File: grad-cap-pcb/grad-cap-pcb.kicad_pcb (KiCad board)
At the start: 2 copper layers, 323.3 x 323.3 mm, 171 parts, among them Q1 NPN, Q10 NPN, Q11 NPN, Q12 NPN, Q13 NPN, Q14 NPN, Q15 NPN, Q16 NPN, Q2 NPN, Q3 NPN, Q4 NPN, Q5 NPN, Q6 NPN, Q7 NPN, Q8 NPN, Q9 NPN, U1 SN74AHCT32DBR, U2 SN74AHCT32DBR, U3 CD4072BM96, U6 CD4075BM96, U8 SN74AHCT32DBR

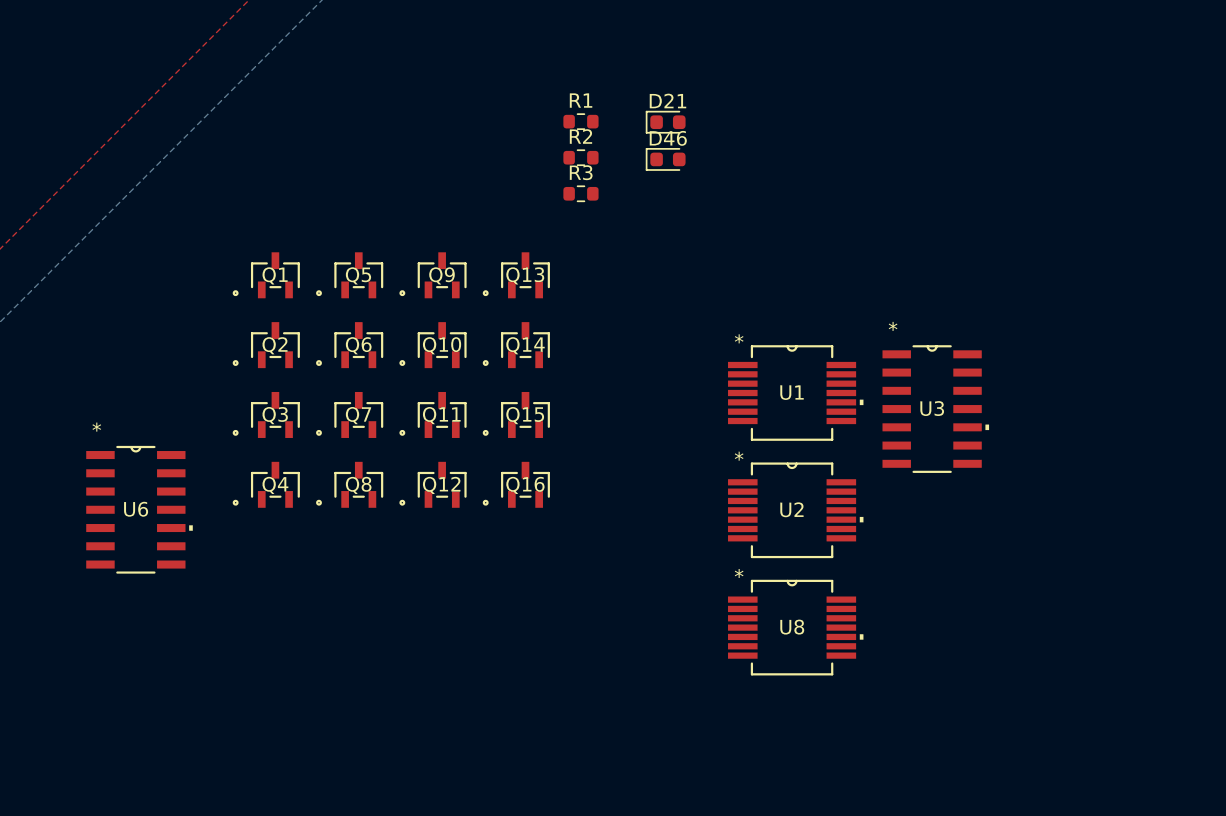
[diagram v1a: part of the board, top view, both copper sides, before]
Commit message: added many things
added: mux
counter
signal gen - still needs r1 and r2 values
power management
kicad symbol library - footprints not assigned
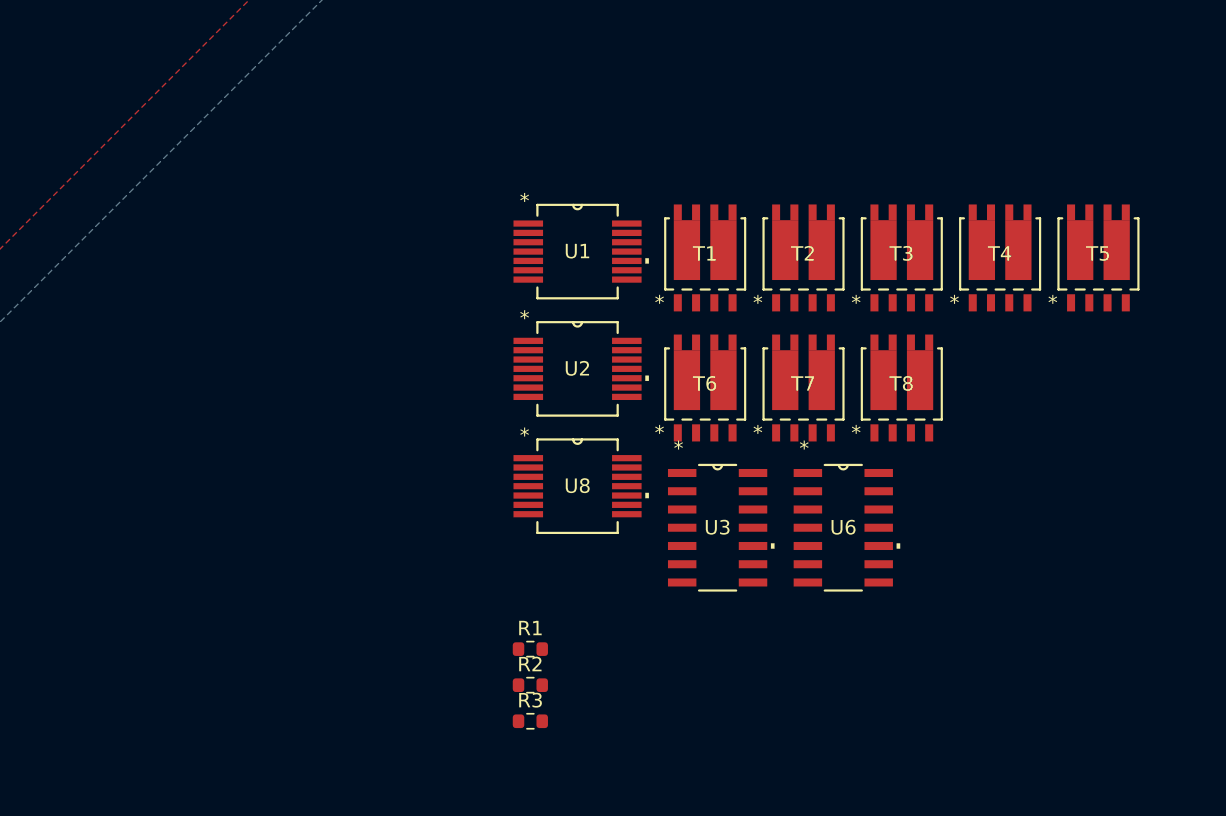
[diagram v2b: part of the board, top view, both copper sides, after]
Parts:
- removed D21, D46: LED, LED_SMD:LED_0603_1608Metric
- removed Q1, Q10, Q11, Q12, Q13, Q14, Q15, Q16, Q2, Q3, Q4, Q5, Q6, Q7, Q8, Q9: NPN, General Library:PN2907A
- added T1: PHPT610035PKX, GRAD-CAP:PHPT610035PKX_TRANS-2PNP-100V-3A, F.Cu at (383.0, 324.2)
- added T2: PHPT610035PKX, GRAD-CAP:PHPT610035PKX_TRANS-2PNP-100V-3A, F.Cu at (389.9, 324.2)
- added T3: PHPT610035PKX, GRAD-CAP:PHPT610035PKX_TRANS-2PNP-100V-3A, F.Cu at (396.7, 324.2)
- added T4: PHPT610035PKX, GRAD-CAP:PHPT610035PKX_TRANS-2PNP-100V-3A, F.Cu at (403.6, 324.2)
- added T5: PHPT610035PKX, GRAD-CAP:PHPT610035PKX_TRANS-2PNP-100V-3A, F.Cu at (410.4, 324.2)
- added T6: PHPT610035PKX, GRAD-CAP:PHPT610035PKX_TRANS-2PNP-100V-3A, F.Cu at (383.0, 333.3)
- added T7: PHPT610035PKX, GRAD-CAP:PHPT610035PKX_TRANS-2PNP-100V-3A, F.Cu at (389.9, 333.3)
- added T8: PHPT610035PKX, GRAD-CAP:PHPT610035PKX_TRANS-2PNP-100V-3A, F.Cu at (396.7, 333.3)
- moved U6 49.2 mm to (392.7, 343.3)
- moved R1 36.9 mm to (370.9, 351.7)
- moved R2 36.9 mm to (370.9, 354.2)
- moved R3 36.9 mm to (370.9, 356.7)
- moved U2 17.9 mm to (374.2, 332.2)
- moved U8 17.9 mm to (374.2, 340.4)
- moved U1 17.9 mm to (374.2, 324.1)
- moved U3 17.1 mm to (383.9, 343.3)
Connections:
- D1 pad 2: +2V2 -> Net-(D1-A)
- D10 pad 2: +2V2 -> Net-(D10-A)
- D100 pad 2: +2V2 -> Net-(D100-A)
- D101 pad 2: +2V2 -> Net-(D100-A)
- D102 pad 2: +2V2 -> Net-(D100-A)
- D103 pad 2: +2V2 -> Net-(D103-A)
- D104 pad 2: +2V2 -> Net-(D103-A)
- D105 pad 2: +2V2 -> Net-(D103-A)
- D106 pad 2: +2V2 -> Net-(D103-A)
- D107 pad 2: +2V2 -> Net-(D103-A)
- D108 pad 2: +2V2 -> Net-(D103-A)
- D109 pad 2: +2V2 -> Net-(D109-A)
- D11 pad 2: +2V2 -> Net-(D10-A)
- D110 pad 2: +2V2 -> Net-(D109-A)
- D111 pad 2: +2V2 -> Net-(D109-A)
- D112 pad 2: +2V2 -> Net-(D109-A)
- D113 pad 2: +2V2 -> Net-(D109-A)
- D114 pad 2: +2V2 -> Net-(D109-A)
- D115 pad 2: +2V2 -> Net-(D115-A)
- D116 pad 2: +2V2 -> Net-(D115-A)
- D117 pad 2: +2V2 -> Net-(D115-A)
- D118 pad 2: +2V2 -> Net-(D115-A)
- D119 pad 2: +2V2 -> Net-(D115-A)
- D12 pad 2: +2V2 -> Net-(D10-A)
- D120 pad 2: +2V2 -> Net-(D115-A)
- D121 pad 2: +2V2 -> Net-(D121-A)
- D122 pad 2: +2V2 -> Net-(D121-A)
- D123 pad 2: +2V2 -> Net-(D121-A)
- D124 pad 2: +2V2 -> Net-(D121-A)
- D125 pad 2: +2V2 -> Net-(D121-A)
- D126 pad 2: +2V2 -> Net-(D121-A)
- D127 pad 2: +2V2 -> Net-(D127-A)
- D128 pad 2: +2V2 -> Net-(D127-A)
- D129 pad 2: +2V2 -> Net-(D127-A)
- D13 pad 2: +2V2 -> Net-(D13-A)
- D130 pad 2: +2V2 -> Net-(D127-A)
- D131 pad 2: +2V2 -> Net-(D127-A)
- D132 pad 2: +2V2 -> Net-(D127-A)
- D133 pad 2: +2V2 -> Net-(D133-A)
- D134 pad 2: +2V2 -> Net-(D133-A)
- D135 pad 2: +2V2 -> Net-(D133-A)
- D136 pad 2: +2V2 -> Net-(D133-A)
- D137 pad 2: +2V2 -> Net-(D133-A)
- D138 pad 2: +2V2 -> Net-(D133-A)
- D139 pad 2: +2V2 -> Net-(D139-A)
- D14 pad 2: +2V2 -> Net-(D13-A)
- D140 pad 2: +2V2 -> Net-(D139-A)
- D141 pad 2: +2V2 -> Net-(D139-A)
- D142 pad 2: +2V2 -> Net-(D139-A)
- D143 pad 2: +2V2 -> Net-(D139-A)
- D144 pad 2: +2V2 -> Net-(D139-A)
- D145 pad 2: +2V2 -> Net-(D145-A)
- D146 pad 2: +2V2 -> Net-(D145-A)
- D147 pad 2: +2V2 -> Net-(D145-A)
- D15 pad 2: +2V2 -> Net-(D13-A)
- D16 pad 2: +2V2 -> Net-(D13-A)
- D17 pad 2: +2V2 -> Net-(D13-A)
- D18 pad 2: +2V2 -> Net-(D13-A)
- D2 pad 2: +2V2 -> Net-(D1-A)
- D20 pad 2: +2V2 -> Net-(D20-A)
- D22 pad 2: +2V2 -> Net-(D20-A)
- D23 pad 2: +2V2 -> Net-(D20-A)
- D24 pad 2: +2V2 -> Net-(D20-A)
- D25 pad 2: +2V2 -> Net-(D20-A)
- D26 pad 2: +2V2 -> Net-(D20-A)
- D27 pad 2: +2V2 -> Net-(D27-A)
- D28 pad 2: +2V2 -> Net-(D27-A)
- D29 pad 2: +2V2 -> Net-(D27-A)
- D3 pad 2: +2V2 -> Net-(D1-A)
- D30 pad 2: +2V2 -> Net-(D27-A)
- D31 pad 2: +2V2 -> Net-(D27-A)
- D32 pad 2: +2V2 -> Net-(D27-A)
- D33 pad 2: +2V2 -> Net-(D33-A)
- D34 pad 2: +2V2 -> Net-(D33-A)
- D35 pad 2: +2V2 -> Net-(D33-A)
- D36 pad 2: +2V2 -> Net-(D33-A)
- D37 pad 2: +2V2 -> Net-(D33-A)
- D38 pad 2: +2V2 -> Net-(D33-A)
- D39 pad 2: +2V2 -> Net-(D39-A)
- D4 pad 2: +2V2 -> Net-(D1-A)
- D40 pad 2: +2V2 -> Net-(D39-A)
- D41 pad 2: +2V2 -> Net-(D39-A)
- D42 pad 2: +2V2 -> Net-(D39-A)
- D43 pad 2: +2V2 -> Net-(D39-A)
- D44 pad 2: +2V2 -> Net-(D39-A)
- D45 pad 2: +2V2 -> Net-(D45-A)
- D47 pad 2: +2V2 -> Net-(D45-A)
- D48 pad 2: +2V2 -> Net-(D45-A)
- D49 pad 2: +2V2 -> Net-(D45-A)
- D5 pad 2: +2V2 -> Net-(D1-A)
- D50 pad 2: +2V2 -> Net-(D45-A)
- D51 pad 2: +2V2 -> Net-(D45-A)
- D52 pad 2: +2V2 -> Net-(D52-A)
- D53 pad 2: +2V2 -> Net-(D52-A)
- D54 pad 2: +2V2 -> Net-(D52-A)
- D55 pad 2: +2V2 -> Net-(D55-A)
- D56 pad 2: +2V2 -> Net-(D55-A)
- D57 pad 2: +2V2 -> Net-(D55-A)
- D58 pad 2: +2V2 -> Net-(D55-A)
- D59 pad 2: +2V2 -> Net-(D55-A)
- D6 pad 2: +2V2 -> Net-(D1-A)
- D60 pad 2: +2V2 -> Net-(D55-A)
- D61 pad 2: +2V2 -> Net-(D61-A)
- D62 pad 2: +2V2 -> Net-(D61-A)
- D63 pad 2: +2V2 -> Net-(D61-A)
- D64 pad 2: +2V2 -> Net-(D61-A)
- D65 pad 2: +2V2 -> Net-(D61-A)
- D66 pad 2: +2V2 -> Net-(D61-A)
- D67 pad 2: +2V2 -> Net-(D67-A)
- D68 pad 2: +2V2 -> Net-(D67-A)
- D69 pad 2: +2V2 -> Net-(D67-A)
- D7 pad 2: +2V2 -> Net-(D10-A)
- D70 pad 2: +2V2 -> Net-(D67-A)
- D71 pad 2: +2V2 -> Net-(D67-A)
- D72 pad 2: +2V2 -> Net-(D67-A)
- D73 pad 2: +2V2 -> Net-(D73-A)
- D74 pad 2: +2V2 -> Net-(D73-A)
- D75 pad 2: +2V2 -> Net-(D73-A)
- D76 pad 2: +2V2 -> Net-(D73-A)
- D77 pad 2: +2V2 -> Net-(D73-A)
- D78 pad 2: +2V2 -> Net-(D73-A)
- D79 pad 2: +2V2 -> Net-(D79-A)
- D8 pad 2: +2V2 -> Net-(D10-A)
- D80 pad 2: +2V2 -> Net-(D79-A)
- D81 pad 2: +2V2 -> Net-(D79-A)
- D82 pad 2: +2V2 -> Net-(D79-A)
- D83 pad 2: +2V2 -> Net-(D79-A)
- D84 pad 2: +2V2 -> Net-(D79-A)
- D85 pad 2: +2V2 -> Net-(D85-A)
- D86 pad 2: +2V2 -> Net-(D85-A)
- D87 pad 2: +2V2 -> Net-(D85-A)
- D88 pad 2: +2V2 -> Net-(D85-A)
- D89 pad 2: +2V2 -> Net-(D85-A)
- D9 pad 2: +2V2 -> Net-(D10-A)
- D90 pad 2: +2V2 -> Net-(D85-A)
- D91 pad 2: +2V2 -> Net-(D91-A)
- D92 pad 2: +2V2 -> Net-(D91-A)
- D93 pad 2: +2V2 -> Net-(D91-A)
- D94 pad 2: +2V2 -> Net-(D91-A)
- D95 pad 2: +2V2 -> Net-(D91-A)
- D96 pad 2: +2V2 -> Net-(D91-A)
- D97 pad 2: +2V2 -> Net-(D100-A)
- D98 pad 2: +2V2 -> Net-(D100-A)
- D99 pad 2: +2V2 -> Net-(D100-A)

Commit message: edited layout
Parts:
- removed D19: LED, LED_SMD:LED_0603_1608Metric
- removed R2, R3: 0 ohms, Resistor_SMD:R_0603_1608Metric
- added C1: C_Small_US, Capacitor_SMD:C_0805_2012Metric_Pad1.18x1.45mm_HandSolder, F.Cu at (223.2, 338.2)
- added C2: C_Small, Capacitor_SMD:C_0805_2012Metric_Pad1.18x1.45mm_HandSolder, F.Cu at (221.1, 340.4)
- added J1: B02B-XASK-1LFSN, GRAD-CAP:1X02JST, F.Cu at (252.5, 370.0)
- added R10: 10k, Resistor_SMD:R_0805_2012Metric_Pad1.20x1.40mm_HandSolder, F.Cu at (243.2, 357.8)
- added R4: R_Small_US, Resistor_SMD:R_0805_2012Metric_Pad1.20x1.40mm_HandSolder, F.Cu at (235.8, 350.0)
- added R5: R_Small_US, Resistor_SMD:R_0805_2012Metric_Pad1.20x1.40mm_HandSolder, F.Cu at (233.7, 352.1)
- added R6: 10K, Resistor_SMD:R_0805_2012Metric_Pad1.20x1.40mm_HandSolder, F.Cu at (208.7, 323.5)
- added R7: 10K, Resistor_SMD:R_0805_2012Metric_Pad1.20x1.40mm_HandSolder, F.Cu at (217.5, 332.4)
- added R8: 10K, Resistor_SMD:R_0805_2012Metric_Pad1.20x1.40mm_HandSolder, F.Cu at (214.3, 329.1)
- added R9: 10K, Resistor_SMD:R_0805_2012Metric_Pad1.20x1.40mm_HandSolder, F.Cu at (205.1, 320.0)
- added U10: CD74HC154M96, GRAD-CAP:CD74HC154M96_4-16-MUX, F.Cu at (233.5, 279.8)
- added U4: MC74HC73ADR2G, GRAD-CAP:MC74HC73ADR2G_JK-FLIPFLOP, F.Cu at (222.8, 323.5)
- added U5: MC74HC73ADR2G, GRAD-CAP:MC74HC73ADR2G_JK-FLIPFLOP, F.Cu at (213.7, 314.4)
- added U7: ICM7555xB, Package_SO:SOIC-8_3.9x4.9mm_P1.27mm, F.Cu at (230.6, 342.9)
- added U9: XC6220B211MR-G, GRAD-CAP:XC6220B21MR_2.1V-1A-REG, F.Cu at (243.7, 361.5)
- R1: value 0 ohms -> 10K; footprint Resistor_SMD:R_0603_1608Metric -> Resistor_SMD:R_0805_2012Metric_Pad1.20x1.40mm_HandSolder
- U1: value SN74AHCT32DBR -> CD4072BM96; footprint GRAD-CAP:SN74AHCT32DBR_2-INPUT-QUAD-OR -> GRAD-CAP:CD4072BM96_4-INPUT-OR
- U2: value SN74AHCT32DBR -> CD4075BM96; footprint GRAD-CAP:SN74AHCT32DBR_2-INPUT-QUAD-OR -> GRAD-CAP:CD4075BM96-3IN-TRIO-OR
- U3: value CD4072BM96 -> SN74AHCT32DBR; footprint GRAD-CAP:CD4072BM96_4-INPUT-OR -> GRAD-CAP:SN74AHCT32DBR_2-INPUT-QUAD-OR
- U6: value CD4075BM96 -> SN74AHCT32DBR; footprint GRAD-CAP:CD4075BM96-3IN-TRIO-OR -> GRAD-CAP:SN74AHCT32DBR_2-INPUT-QUAD-OR
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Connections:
- D1 pad 1: /leds+mosfets/frame1 -> GND
- D1 pad 2: Net-(D1-A) -> /leds+mosfets/frame1
- D10 pad 1: /leds+mosfets/frame4 -> GND
- D10 pad 2: Net-(D10-A) -> /leds+mosfets/frame4
- D100 pad 1: /leds+mosfets/frame14 -> GND
- D100 pad 2: Net-(D100-A) -> /leds+mosfets/frame14
- D101 pad 1: /leds+mosfets/frame15 -> GND
- D101 pad 2: Net-(D100-A) -> /leds+mosfets/15or16
- D102 pad 1: /leds+mosfets/13or14 -> GND
- D102 pad 2: Net-(D100-A) -> /leds+mosfets/13or14
- D103 pad 1: /leds+mosfets/frame14 -> GND
- D103 pad 2: Net-(D103-A) -> unconnected-(D103-A-Pad2)
- D104 pad 1: /leds+mosfets/14or15 -> GND
- D104 pad 2: Net-(D103-A) -> /leds+mosfets/frame15
- D105 pad 1: /leds+mosfets/frame15 -> GND
- D105 pad 2: Net-(D103-A) -> /leds+mosfets/frame15
- D106 pad 1: /leds+mosfets/15or16 -> GND
- D106 pad 2: Net-(D103-A) -> /leds+mosfets/15or16
- D107 pad 1: /leds+mosfets/frame16 -> GND
- D107 pad 2: Net-(D103-A) -> /leds+mosfets/frame16
- D108 pad 1: /leds+mosfets/frame1 -> GND
- D108 pad 2: Net-(D103-A) -> /leds+mosfets/frame1
- D109 pad 1: /leds+mosfets/frame1 -> GND
- D109 pad 2: Net-(D109-A) -> /leds+mosfets/frame1
- D11 pad 1: /leds+mosfets/frame4 -> GND
- D11 pad 2: Net-(D10-A) -> /leds+mosfets/frame4
- D110 pad 1: /leds+mosfets/frame2 -> GND
- D110 pad 2: Net-(D109-A) -> /leds+mosfets/frame2
- D111 pad 1: /leds+mosfets/frame3 -> GND
- D111 pad 2: Net-(D109-A) -> /leds+mosfets/frame3
- D112 pad 1: /leds+mosfets/frame3 -> GND
- D112 pad 2: Net-(D109-A) -> /leds+mosfets/frame3
- D113 pad 1: /leds+mosfets/3or4 -> GND
- D113 pad 2: Net-(D109-A) -> /leds+mosfets/3or4
- D114 pad 1: /leds+mosfets/frame4 -> GND
- D114 pad 2: Net-(D109-A) -> /leds+mosfets/frame4
- D115 pad 1: /leds+mosfets/frame3 -> GND
- D115 pad 2: Net-(D115-A) -> /leds+mosfets/frame3
- D116 pad 1: /leds+mosfets/frame4 -> GND
- D116 pad 2: Net-(D115-A) -> /leds+mosfets/frame4
- D117 pad 1: /leds+mosfets/frame4 -> GND
- D117 pad 2: Net-(D115-A) -> /leds+mosfets/frame4
- D118 pad 1: /leds+mosfets/frame4 -> GND
- D118 pad 2: Net-(D115-A) -> /leds+mosfets/frame4
- D119 pad 1: /leds+mosfets/frame3 -> GND
- D119 pad 2: Net-(D115-A) -> /leds+mosfets/frame3
- D12 pad 1: /leds+mosfets/frame4 -> GND
- D12 pad 2: Net-(D10-A) -> /leds+mosfets/frame4
- D120 pad 1: /leds+mosfets/frame4 -> GND
- D120 pad 2: Net-(D115-A) -> /leds+mosfets/frame4
- D121 pad 1: /leds+mosfets/4or5 -> GND
- D121 pad 2: Net-(D121-A) -> /leds+mosfets/4or5
- D122 pad 1: /leds+mosfets/4or5 -> GND
- D122 pad 2: Net-(D121-A) -> /leds+mosfets/4or5
- D123 pad 1: /leds+mosfets/frame4 -> GND
- D123 pad 2: Net-(D121-A) -> /leds+mosfets/frame4
- D124 pad 1: /leds+mosfets/4or5 -> GND
- D124 pad 2: Net-(D121-A) -> /leds+mosfets/4or5
- D125 pad 1: /leds+mosfets/4or5 -> GND
- D125 pad 2: Net-(D121-A) -> /leds+mosfets/4or5
- D126 pad 1: /leds+mosfets/4or5 -> GND
- D126 pad 2: Net-(D121-A) -> /leds+mosfets/4or5
- D127 pad 1: /leds+mosfets/frame5 -> GND
- D127 pad 2: Net-(D127-A) -> /leds+mosfets/frame5
- D128 pad 1: /leds+mosfets/4or5 -> GND
- D128 pad 2: Net-(D127-A) -> /leds+mosfets/4or5
- D129 pad 1: /leds+mosfets/frame4 -> GND
- D129 pad 2: Net-(D127-A) -> /leds+mosfets/frame4
- D13 pad 1: /leds+mosfets/4or5 -> GND
- D13 pad 2: Net-(D13-A) -> /leds+mosfets/4or5
- D130 pad 1: /leds+mosfets/5or6 -> GND
- D130 pad 2: Net-(D127-A) -> /leds+mosfets/5or6
- D131 pad 1: /leds+mosfets/5or6 -> GND
- D131 pad 2: Net-(D127-A) -> /leds+mosfets/5or6
- D132 pad 1: /leds+mosfets/5or6 -> GND
- D132 pad 2: Net-(D127-A) -> /leds+mosfets/5or6
- D133 pad 1: /leds+mosfets/4or5 -> GND
- D133 pad 2: Net-(D133-A) -> /leds+mosfets/4or5
- D134 pad 1: /leds+mosfets/frame6 -> GND
- D134 pad 2: Net-(D133-A) -> /leds+mosfets/frame6
- D135 pad 1: /leds+mosfets/5or6 -> GND
- D135 pad 2: Net-(D133-A) -> /leds+mosfets/5or6
- D136 pad 1: /leds+mosfets/5or6 -> GND
- D136 pad 2: Net-(D133-A) -> /leds+mosfets/5or6
- D137 pad 1: /leds+mosfets/5or6 -> GND
- D137 pad 2: Net-(D133-A) -> /leds+mosfets/5or6
- D138 pad 1: /leds+mosfets/5or6 -> GND
- D138 pad 2: Net-(D133-A) -> /leds+mosfets/5or6
- D139 pad 1: /leds+mosfets/6or7 -> GND
- D139 pad 2: Net-(D139-A) -> /leds+mosfets/6or7
- D14 pad 1: /leds+mosfets/frame5 -> GND
- D14 pad 2: Net-(D13-A) -> /leds+mosfets/frame5
- D140 pad 1: /leds+mosfets/6or7 -> GND
- D140 pad 2: Net-(D139-A) -> /leds+mosfets/6or7
- D141 pad 1: /leds+mosfets/6or7 -> GND
- D141 pad 2: Net-(D139-A) -> /leds+mosfets/6or7
- D142 pad 1: /leds+mosfets/5or6or7or8 -> GND
- D142 pad 2: Net-(D139-A) -> /leds+mosfets/5or6or7or8
- D143 pad 1: /leds+mosfets/6or7or8 -> GND
- D143 pad 2: Net-(D139-A) -> /leds+mosfets/6or7or8
- D144 pad 1: /leds+mosfets/6or7or8 -> GND
- D144 pad 2: Net-(D139-A) -> /leds+mosfets/6or7or8
- D145 pad 1: /leds+mosfets/6or7 -> GND
- D145 pad 2: Net-(D145-A) -> /leds+mosfets/6or7
- D146 pad 1: /leds+mosfets/7or8 -> GND
- D146 pad 2: Net-(D145-A) -> /leds+mosfets/7or8
- D147 pad 1: /leds+mosfets/frame7 -> GND
- D147 pad 2: Net-(D145-A) -> /leds+mosfets/frame7
- D15 pad 1: /leds+mosfets/4or5 -> GND
- D15 pad 2: Net-(D13-A) -> /leds+mosfets/4or5
- D16 pad 1: /leds+mosfets/4or5 -> GND
- D16 pad 2: Net-(D13-A) -> /leds+mosfets/4or5
- D17 pad 1: /leds+mosfets/frame5 -> GND
- D17 pad 2: Net-(D13-A) -> /leds+mosfets/frame5
- D18 pad 1: /leds+mosfets/frame4 -> GND
- D18 pad 2: Net-(D13-A) -> /leds+mosfets/frame4
- D2 pad 1: /leds+mosfets/frame1 -> GND
- D2 pad 2: Net-(D1-A) -> /leds+mosfets/frame1
- D20 pad 1: /leds+mosfets/6or7 -> GND
- D20 pad 2: Net-(D20-A) -> /leds+mosfets/6or7
- D22 pad 1: /leds+mosfets/6or7 -> GND
- D22 pad 2: Net-(D20-A) -> /leds+mosfets/6or7
- D23 pad 1: /leds+mosfets/frame6 -> GND
- D23 pad 2: Net-(D20-A) -> /leds+mosfets/frame6
- D24 pad 1: /leds+mosfets/frame6 -> GND
- D24 pad 2: Net-(D20-A) -> /leds+mosfets/frame6
- D25 pad 1: /leds+mosfets/frame6 -> GND
- D25 pad 2: Net-(D20-A) -> /leds+mosfets/frame6
- D26 pad 1: /leds+mosfets/frame6 -> GND
- D26 pad 2: Net-(D20-A) -> /leds+mosfets/frame6
- D27 pad 1: /leds+mosfets/6or7 -> GND
- D27 pad 2: Net-(D27-A) -> /leds+mosfets/6or7
- D28 pad 1: /leds+mosfets/6or7 -> GND
- D28 pad 2: Net-(D27-A) -> /leds+mosfets/6or7
- D29 pad 1: /leds+mosfets/frame7 -> GND
- D29 pad 2: Net-(D27-A) -> /leds+mosfets/frame7
- D3 pad 1: /leds+mosfets/frame2 -> GND
- D3 pad 2: Net-(D1-A) -> /leds+mosfets/frame2
- D30 pad 1: /leds+mosfets/7or8 -> GND
- D30 pad 2: Net-(D27-A) -> /leds+mosfets/7or8
- D31 pad 1: /leds+mosfets/7or8 -> GND
- D31 pad 2: Net-(D27-A) -> /leds+mosfets/7or8
- D32 pad 1: /leds+mosfets/6or7 -> GND
- D32 pad 2: Net-(D27-A) -> /leds+mosfets/6or7
- D33 pad 1: /leds+mosfets/7or8 -> GND
- D33 pad 2: Net-(D33-A) -> /leds+mosfets/7or8
- D34 pad 1: /leds+mosfets/6or7 -> GND
- D34 pad 2: Net-(D33-A) -> /leds+mosfets/6or7
- D35 pad 1: /leds+mosfets/frame6 -> GND
- D35 pad 2: Net-(D33-A) -> /leds+mosfets/frame6
- D36 pad 1: /leds+mosfets/7or8 -> GND
- D36 pad 2: Net-(D33-A) -> /leds+mosfets/7or8
- D37 pad 1: /leds+mosfets/7or8 -> GND
- D37 pad 2: Net-(D33-A) -> /leds+mosfets/7or8
- D38 pad 1: /leds+mosfets/frame7 -> GND
- D38 pad 2: Net-(D33-A) -> /leds+mosfets/frame7
- D39 pad 1: /leds+mosfets/7or8 -> GND
- D39 pad 2: Net-(D39-A) -> /leds+mosfets/7or8
- D4 pad 1: /leds+mosfets/frame2 -> GND
- D4 pad 2: Net-(D1-A) -> /leds+mosfets/frame2
- D40 pad 1: /leds+mosfets/8or9 -> GND
- D40 pad 2: Net-(D39-A) -> /leds+mosfets/8or9
- D41 pad 1: /leds+mosfets/8or9 -> GND
- D41 pad 2: Net-(D39-A) -> /leds+mosfets/8or9
- D42 pad 1: /leds+mosfets/8or9 -> GND
- D42 pad 2: Net-(D39-A) -> /leds+mosfets/8or9
- D43 pad 1: /leds+mosfets/7or8or9 -> GND
- D43 pad 2: Net-(D39-A) -> /leds+mosfets/7or8or9
- D44 pad 1: /leds+mosfets/8or9 -> GND
- D44 pad 2: Net-(D39-A) -> /leds+mosfets/8or9
- D45 pad 1: /leds+mosfets/frame7 -> GND
- D45 pad 2: Net-(D45-A) -> /leds+mosfets/frame7
- D47 pad 1: /leds+mosfets/frame9 -> GND
- D47 pad 2: Net-(D45-A) -> /leds+mosfets/frame9
- D48 pad 1: /leds+mosfets/7or8 -> GND
- D48 pad 2: Net-(D45-A) -> /leds+mosfets/7or8
- D49 pad 1: /leds+mosfets/7or8 -> GND
- D49 pad 2: Net-(D45-A) -> /leds+mosfets/7or8
- D5 pad 1: /leds+mosfets/frame3 -> GND
- D5 pad 2: Net-(D1-A) -> /leds+mosfets/frame3
- D50 pad 1: /leds+mosfets/9or10 -> GND
- D50 pad 2: Net-(D45-A) -> /leds+mosfets/9or10
- D51 pad 1: /leds+mosfets/8or9or10 -> GND
- D51 pad 2: Net-(D45-A) -> /leds+mosfets/8or9or10
- D52 pad 1: /leds+mosfets/7or8or9 -> GND
- D52 pad 2: Net-(D52-A) -> /leds+mosfets/7or8or9
- D53 pad 1: /leds+mosfets/7or8 -> GND
- D53 pad 2: Net-(D52-A) -> /leds+mosfets/7or8
- D54 pad 1: /leds+mosfets/frame9 -> GND
- D54 pad 2: Net-(D52-A) -> /leds+mosfets/frame9
- D55 pad 1: /leds+mosfets/frame7 -> GND
- D55 pad 2: Net-(D55-A) -> /leds+mosfets/frame7
- D56 pad 1: /leds+mosfets/7or8 -> GND
- D56 pad 2: Net-(D55-A) -> /leds+mosfets/7or8
- D57 pad 1: /leds+mosfets/frame8 -> GND
- D57 pad 2: Net-(D55-A) -> /leds+mosfets/frame8
- D58 pad 1: /leds+mosfets/frame9 -> GND
- D58 pad 2: Net-(D55-A) -> /leds+mosfets/frame9
- D59 pad 1: /leds+mosfets/frame9 -> GND
- D59 pad 2: Net-(D55-A) -> /leds+mosfets/frame9
- D6 pad 1: /leds+mosfets/frame3 -> GND
- D6 pad 2: Net-(D1-A) -> /leds+mosfets/frame3
- D60 pad 1: /leds+mosfets/10or11 -> GND
- D60 pad 2: Net-(D55-A) -> /leds+mosfets/frame10
- D61 pad 1: /leds+mosfets/frame11 -> GND
- D61 pad 2: Net-(D61-A) -> /leds+mosfets/frame11
- D62 pad 1: /leds+mosfets/frame11 -> GND
- D62 pad 2: Net-(D61-A) -> /leds+mosfets/frame11
- D63 pad 1: /leds+mosfets/frame12 -> GND
- D63 pad 2: Net-(D61-A) -> /leds+mosfets/frame12
- D64 pad 1: /leds+mosfets/frame12 -> GND
- D64 pad 2: Net-(D61-A) -> /leds+mosfets/frame12
- D65 pad 1: /leds+mosfets/frame12 -> GND
- D65 pad 2: Net-(D61-A) -> /leds+mosfets/frame12
- D66 pad 1: /leds+mosfets/frame12 -> GND
- D66 pad 2: Net-(D61-A) -> /leds+mosfets/frame12
- D67 pad 1: /leds+mosfets/frame12 -> GND
- D67 pad 2: Net-(D67-A) -> /leds+mosfets/frame12
- D68 pad 1: /leds+mosfets/12or13 -> GND
- D68 pad 2: Net-(D67-A) -> /leds+mosfets/12or13
- D69 pad 1: /leds+mosfets/frame13 -> GND
- D69 pad 2: Net-(D67-A) -> /leds+mosfets/frame13
- D7 pad 1: /leds+mosfets/frame4 -> GND
- D7 pad 2: Net-(D10-A) -> /leds+mosfets/frame4
- D70 pad 1: /leds+mosfets/frame13 -> GND
- D70 pad 2: Net-(D67-A) -> /leds+mosfets/frame13
- D71 pad 1: /leds+mosfets/frame13 -> GND
- D71 pad 2: Net-(D67-A) -> /leds+mosfets/frame13
- D72 pad 1: /leds+mosfets/12or13 -> GND
- D72 pad 2: Net-(D67-A) -> /leds+mosfets/12or13
- D73 pad 1: /leds+mosfets/frame12 -> GND
- D73 pad 2: Net-(D73-A) -> /leds+mosfets/frame12
- D74 pad 1: /leds+mosfets/frame13 -> GND
- D74 pad 2: Net-(D73-A) -> /leds+mosfets/frame13
- D75 pad 1: /leds+mosfets/frame14 -> GND
- D75 pad 2: Net-(D73-A) -> /leds+mosfets/frame14
- D76 pad 1: /leds+mosfets/frame13 -> GND
- D76 pad 2: Net-(D73-A) -> /leds+mosfets/frame13
- D77 pad 1: /leds+mosfets/13or14 -> GND
- D77 pad 2: Net-(D73-A) -> /leds+mosfets/13or14
- D78 pad 1: /leds+mosfets/frame13 -> GND
- D78 pad 2: Net-(D73-A) -> /leds+mosfets/frame13
- D79 pad 1: /leds+mosfets/frame13 -> GND
- D79 pad 2: Net-(D79-A) -> /leds+mosfets/frame13
- D8 pad 1: /leds+mosfets/frame4 -> GND
- D8 pad 2: Net-(D10-A) -> /leds+mosfets/frame4
- D80 pad 1: /leds+mosfets/frame14 -> GND
- D80 pad 2: Net-(D79-A) -> /leds+mosfets/frame14
- D81 pad 1: /leds+mosfets/frame13 -> GND
- D81 pad 2: Net-(D79-A) -> /leds+mosfets/frame13
- D82 pad 1: /leds+mosfets/frame14 -> GND
- D82 pad 2: Net-(D79-A) -> /leds+mosfets/frame14
- D83 pad 1: /leds+mosfets/12or13 -> GND
- D83 pad 2: Net-(D79-A) -> /leds+mosfets/12or13
- D84 pad 1: /leds+mosfets/13or14 -> GND
- D84 pad 2: Net-(D79-A) -> /leds+mosfets/13or14
- D85 pad 1: /leds+mosfets/14or15 -> GND
- D85 pad 2: Net-(D85-A) -> /leds+mosfets/14or15
- D86 pad 1: /leds+mosfets/13or14 -> GND
- D86 pad 2: Net-(D85-A) -> /leds+mosfets/13or14
- D87 pad 1: /leds+mosfets/14or15 -> GND
- D87 pad 2: Net-(D85-A) -> /leds+mosfets/14or15
- D88 pad 1: /leds+mosfets/frame14 -> GND
- D88 pad 2: Net-(D85-A) -> /leds+mosfets/frame14
- D89 pad 1: /leds+mosfets/frame14 -> GND
- D89 pad 2: Net-(D85-A) -> /leds+mosfets/frame14
- D9 pad 1: /leds+mosfets/frame4 -> GND
- D9 pad 2: Net-(D10-A) -> /leds+mosfets/frame4
- D90 pad 1: /leds+mosfets/14or15 -> GND
- D90 pad 2: Net-(D85-A) -> /leds+mosfets/14or15
- D91 pad 1: /leds+mosfets/frame14 -> GND
- D91 pad 2: Net-(D91-A) -> /leds+mosfets/frame14
- D92 pad 1: /leds+mosfets/frame15 -> GND
- D92 pad 2: Net-(D91-A) -> /leds+mosfets/frame15
- D93 pad 1: /leds+mosfets/frame13 -> GND
- D93 pad 2: Net-(D91-A) -> /leds+mosfets/frame13
- D94 pad 1: /leds+mosfets/14or15 -> GND
- D94 pad 2: Net-(D91-A) -> /leds+mosfets/14or15
- D95 pad 1: /leds+mosfets/frame16 -> GND
- D95 pad 2: Net-(D91-A) -> /leds+mosfets/15or16
- D96 pad 1: /leds+mosfets/14or15 -> GND
- D96 pad 2: Net-(D91-A) -> /leds+mosfets/14or15
- D97 pad 1: /leds+mosfets/frame14 -> GND
- D97 pad 2: Net-(D100-A) -> /leds+mosfets/frame14
- D98 pad 1: /leds+mosfets/frame15 -> GND
- D98 pad 2: Net-(D100-A) -> /leds+mosfets/frame15
- D99 pad 1: /leds+mosfets/15or16 -> GND
- D99 pad 2: Net-(D100-A) -> /leds+mosfets/15or16
- R1 pad 2: unconnected-(R1-Pad2) -> GND
- T1 pad 2: 0 -> 1
- T1 pad 4: 1 -> 0
- T1 pad 5: /leds+mosfets/frame2 -> /leds+mosfets/frame1
- T1 pad 6: /leds+mosfets/frame2 -> /leds+mosfets/frame1
- T1 pad 7: /leds+mosfets/frame1 -> /leds+mosfets/frame2
- T1 pad 8: /leds+mosfets/frame1 -> /leds+mosfets/frame2
- T2 pad 2: 2 -> 3
- T2 pad 4: 3 -> 2
- T2 pad 5: /leds+mosfets/frame4 -> /leds+mosfets/frame3
- T2 pad 6: /leds+mosfets/frame4 -> /leds+mosfets/frame3
- T2 pad 7: /leds+mosfets/frame3 -> /leds+mosfets/frame4
- T2 pad 8: /leds+mosfets/frame3 -> /leds+mosfets/frame4
- T3 pad 2: 4 -> 5
- T3 pad 4: 5 -> 4
- T3 pad 5: /leds+mosfets/frame6 -> /leds+mosfets/frame5
- T3 pad 6: /leds+mosfets/frame6 -> /leds+mosfets/frame5
- T3 pad 7: /leds+mosfets/frame5 -> /leds+mosfets/frame6
- T3 pad 8: /leds+mosfets/frame5 -> /leds+mosfets/frame6
- T4 pad 2: 6 -> 7
- T4 pad 4: 7 -> 6
- T4 pad 5: /leds+mosfets/frame8 -> /leds+mosfets/frame7
- T4 pad 6: /leds+mosfets/frame8 -> /leds+mosfets/frame7
- T4 pad 7: /leds+mosfets/frame7 -> /leds+mosfets/frame8
- T4 pad 8: /leds+mosfets/frame7 -> /leds+mosfets/frame8
- T5 pad 2: 8 -> 9
- T5 pad 4: 9 -> 8
- T5 pad 5: /leds+mosfets/frame10 -> /leds+mosfets/frame9
- T5 pad 6: /leds+mosfets/frame10 -> /leds+mosfets/frame9
- T5 pad 7: /leds+mosfets/frame9 -> /leds+mosfets/frame10
- T5 pad 8: /leds+mosfets/frame9 -> /leds+mosfets/frame10
- T6 pad 2: 10 -> 11
- T6 pad 4: 11 -> 10
- T6 pad 5: /leds+mosfets/frame12 -> /leds+mosfets/frame11
- T6 pad 6: /leds+mosfets/frame12 -> /leds+mosfets/frame11
- T6 pad 7: /leds+mosfets/frame11 -> /leds+mosfets/frame12
- T6 pad 8: /leds+mosfets/frame11 -> /leds+mosfets/frame12
- T7 pad 2: 12 -> 13
- T7 pad 4: 13 -> 12
- T7 pad 5: /leds+mosfets/frame14 -> /leds+mosfets/frame13
- T7 pad 6: /leds+mosfets/frame14 -> /leds+mosfets/frame13
- T7 pad 7: /leds+mosfets/frame13 -> /leds+mosfets/frame14
- T7 pad 8: /leds+mosfets/frame13 -> /leds+mosfets/frame14
- T8 pad 2: 14 -> 15
- T8 pad 4: 15 -> 14
- T8 pad 5: /leds+mosfets/frame16 -> /leds+mosfets/frame15
- T8 pad 6: /leds+mosfets/frame16 -> /leds+mosfets/frame15
- T8 pad 7: /leds+mosfets/frame15 -> /leds+mosfets/frame16
- T8 pad 8: /leds+mosfets/frame15 -> /leds+mosfets/frame16
- U1 pad 1: /leds+mosfets/frame13 -> /leds+mosfets/5or6or7or8
- U1 pad 10: /leds+mosfets/frame9 -> /leds+mosfets/frame8
- U1 pad 11: /leds+mosfets/15or16 -> /leds+mosfets/frame7
- U1 pad 12: /leds+mosfets/frame16 -> /leds+mosfets/frame6
- U1 pad 13: /leds+mosfets/frame15 -> /leds+mosfets/6or7or8
- U1 pad 2: /leds+mosfets/frame14 -> /leds+mosfets/frame5
- U1 pad 3: /leds+mosfets/13or14 -> /leds+mosfets/frame6
- U1 pad 4: /leds+mosfets/frame14 -> /leds+mosfets/frame7
- U1 pad 5: /leds+mosfets/frame15 -> /leds+mosfets/frame8
- U1 pad 6: /leds+mosfets/14or15 -> unconnected-(U1-NC-Pad6)
- U1 pad 8: /leds+mosfets/9or10 -> unconnected-(U1-NC-Pad8)
- U1 pad 9: /leds+mosfets/frame10 -> GND
- U2 pad 1: /leds+mosfets/frame7 -> /leds+mosfets/frame10
- U2 pad 10: /leds+mosfets/frame10 -> /leds+mosfets/16or1
- U2 pad 11: /leds+mosfets/8or9 -> /leds+mosfets/frame1
- U2 pad 12: /leds+mosfets/frame9 -> /leds+mosfets/frame16
- U2 pad 13: /leds+mosfets/frame8 -> GND
- U2 pad 2: /leds+mosfets/frame8 -> /leds+mosfets/frame9
- U2 pad 3: /leds+mosfets/7or8 -> /leds+mosfets/frame7
- U2 pad 4: /leds+mosfets/frame6 -> /leds+mosfets/frame8
- U2 pad 5: /leds+mosfets/frame7 -> /leds+mosfets/frame9
- U2 pad 6: /leds+mosfets/6or7 -> /leds+mosfets/7or8or9
- U2 pad 7: GND -> unconnected-(U2-VSS-Pad7)
- U2 pad 8: /leds+mosfets/10or11 -> /leds+mosfets/frame8
- U2 pad 9: /leds+mosfets/frame11 -> /leds+mosfets/8or9or10
- U3 pad 1: /leds+mosfets/5or6or7or8 -> /leds+mosfets/frame3
- U3 pad 10: /leds+mosfets/frame8 -> /leds+mosfets/frame12
- U3 pad 11: /leds+mosfets/frame7 -> /leds+mosfets/4or5
- U3 pad 12: /leds+mosfets/frame6 -> /leds+mosfets/frame5
- U3 pad 13: /leds+mosfets/6or7or8 -> /leds+mosfets/frame4
- U3 pad 2: /leds+mosfets/frame5 -> /leds+mosfets/frame4
- U3 pad 3: /leds+mosfets/frame6 -> /leds+mosfets/3or4
- U3 pad 4: /leds+mosfets/frame7 -> /leds+mosfets/frame5
- U3 pad 5: /leds+mosfets/frame8 -> /leds+mosfets/frame6
- U3 pad 6: unconnected-(U3-NC-Pad6) -> /leds+mosfets/5or6
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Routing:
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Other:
- board size 323.3 x 323.3 mm -> 339.4 x 339.4 mm
- board text added: "24 cm"
- board text added: "little bigger than 2 cm"

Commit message: routed traces, added resistors
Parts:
- added R11: R_Small_US, Resistor_SMD:R_0805_2012Metric_Pad1.20x1.40mm_HandSolder, F.Cu at (260.0, 290.0)
- added R12: R_Small_US, Resistor_SMD:R_0805_2012Metric_Pad1.20x1.40mm_HandSolder, F.Cu at (260.0, 287.0)
- added R13: R_Small_US, Resistor_SMD:R_0805_2012Metric_Pad1.20x1.40mm_HandSolder, F.Cu at (260.0, 284.0)
- added R14: R_Small_US, Resistor_SMD:R_0805_2012Metric_Pad1.20x1.40mm_HandSolder, F.Cu at (259.9, 280.5)
- added R15: R_Small_US, Resistor_SMD:R_0805_2012Metric_Pad1.20x1.40mm_HandSolder, F.Cu at (260.4, 274.4)
- added R16: R_Small_US, Resistor_SMD:R_0805_2012Metric_Pad1.20x1.40mm_HandSolder, F.Cu at (260.5, 271.0)
- added R17: R_Small_US, Resistor_SMD:R_0805_2012Metric_Pad1.20x1.40mm_HandSolder, F.Cu at (260.2, 267.0)
- added R18: R_Small_US, Resistor_SMD:R_0805_2012Metric_Pad1.20x1.40mm_HandSolder, F.Cu at (256.0, 260.0)
- added R19: R_Small_US, Resistor_SMD:R_0805_2012Metric_Pad1.20x1.40mm_HandSolder, F.Cu at (226.3, 256.1)
- added R2: R_Small_US, Resistor_SMD:R_0805_2012Metric_Pad1.20x1.40mm_HandSolder, F.Cu at (256.0, 301.0)
- added R20: R_Small_US, Resistor_SMD:R_0805_2012Metric_Pad1.20x1.40mm_HandSolder, F.Cu at (217.6, 253.3)
- added R21: R_Small_US, Resistor_SMD:R_0805_2012Metric_Pad1.20x1.40mm_HandSolder, F.Cu at (204.8, 262.4)
- added R22: R_Small_US, Resistor_SMD:R_0805_2012Metric_Pad1.20x1.40mm_HandSolder, F.Cu at (200.0, 269.9)
- added R23: R_Small_US, Resistor_SMD:R_0805_2012Metric_Pad1.20x1.40mm_HandSolder, F.Cu at (199.9, 279.8)
- added R24: R_Small_US, Resistor_SMD:R_0805_2012Metric_Pad1.20x1.40mm_HandSolder, F.Cu at (204.6, 287.0)
- added R25: R_Small_US, Resistor_SMD:R_0805_2012Metric_Pad1.20x1.40mm_HandSolder, F.Cu at (279.0, 262.0)
- added R26: R_Small_US, Resistor_SMD:R_0805_2012Metric_Pad1.20x1.40mm_HandSolder, F.Cu at (319.0, 243.0)
- added R27: R_Small_US, Resistor_SMD:R_0805_2012Metric_Pad1.20x1.40mm_HandSolder, F.Cu at (279.0, 266.0)
- added R28: R_Small_US, Resistor_SMD:R_0805_2012Metric_Pad1.20x1.40mm_HandSolder, F.Cu at (128.0, 226.0)
- added R29: R_Small_US, Resistor_SMD:R_0805_2012Metric_Pad1.20x1.40mm_HandSolder, F.Cu at (300.0, 242.0)
- added R3: R_Small_US, Resistor_SMD:R_0805_2012Metric_Pad1.20x1.40mm_HandSolder, F.Cu at (260.0, 294.0)
- added R30: R_Small_US, Resistor_SMD:R_0805_2012Metric_Pad1.20x1.40mm_HandSolder, F.Cu at (299.0, 263.0)
- added R31: R_Small_US, Resistor_SMD:R_0805_2012Metric_Pad1.20x1.40mm_HandSolder, F.Cu at (111.0, 228.0)
- added R32: R_Small_US, Resistor_SMD:R_0805_2012Metric_Pad1.20x1.40mm_HandSolder, F.Cu at (111.0, 224.0)
- added R33: R_Small_US, Resistor_SMD:R_0805_2012Metric_Pad1.20x1.40mm_HandSolder, F.Cu at (299.0, 267.0)
- added R34: R_Small_US, Resistor_SMD:R_0805_2012Metric_Pad1.20x1.40mm_HandSolder, F.Cu at (209.0, 244.0)
- added R35: R_Small_US, Resistor_SMD:R_0805_2012Metric_Pad1.20x1.40mm_HandSolder, F.Cu at (209.0, 247.6)
- added R36: R_Small_US, Resistor_SMD:R_0805_2012Metric_Pad1.20x1.40mm_HandSolder, F.Cu at (176.0, 252.0)
- added R37: R_Small_US, Resistor_SMD:R_0805_2012Metric_Pad1.20x1.40mm_HandSolder, F.Cu at (228.0, 245.0)
- added R38: R_Small_US, Resistor_SMD:R_0805_2012Metric_Pad1.20x1.40mm_HandSolder, F.Cu at (228.0, 249.0)
- added R39: R_Small_US, Resistor_SMD:R_0805_2012Metric_Pad1.20x1.40mm_HandSolder, F.Cu at (193.0, 253.0)
- added R40: R_Small_US, Resistor_SMD:R_0805_2012Metric_Pad1.20x1.40mm_HandSolder, F.Cu at (176.0, 256.0)
- moved R5 35.9 mm to (243.5, 317.5), turned to -135 degrees
- moved C1 31.3 mm to (232.8, 308.4), turned to 45 degrees
- moved R4 29.1 mm to (239.8, 321.2), turned to -135 degrees
- moved U7 28.0 mm to (234.3, 315.2)
- moved C2 21.5 mm to (233.9, 323.1), turned to -135 degrees
- moved R8 21.3 mm to (217.8, 308.1)
- moved R9 21.3 mm to (208.8, 299.0)
- moved R7 20.9 mm to (221.3, 311.8)
- moved R6 20.9 mm to (212.4, 302.9)
- moved U4 20.9 mm to (226.6, 302.9)
- moved U5 20.9 mm to (217.5, 293.8)
- moved R1 12.2 mm to (224.8, 280.2), turned to 180 degrees
- moved T7 5.82 mm to (207.6, 268.4), turned to 90 degrees
- moved T8 5.33 mm to (207.6, 281.2)
- moved T6 2.48 mm to (220.6, 259.4)
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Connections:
- net Net-(U10-*E1) renamed /pd_r_18/19
- T1 pad 5: /leds+mosfets/frame1 -> /leds+mosfets/0frame1
- T1 pad 6: /leds+mosfets/frame1 -> /leds+mosfets/0frame1
- T1 pad 7: /leds+mosfets/frame2 -> /leds+mosfets/0frame2
- T1 pad 8: /leds+mosfets/frame2 -> /leds+mosfets/0frame2
- T2 pad 5: /leds+mosfets/frame3 -> /leds+mosfets/0frame3
- T2 pad 6: /leds+mosfets/frame3 -> /leds+mosfets/0frame3
- T2 pad 7: /leds+mosfets/frame4 -> /leds+mosfets/0frame4
- T2 pad 8: /leds+mosfets/frame4 -> /leds+mosfets/0frame4
- T3 pad 5: /leds+mosfets/frame5 -> /leds+mosfets/0frame5
- T3 pad 6: /leds+mosfets/frame5 -> /leds+mosfets/0frame5
- T3 pad 7: /leds+mosfets/frame6 -> /leds+mosfets/0frame6
- T3 pad 8: /leds+mosfets/frame6 -> /leds+mosfets/0frame6
- T4 pad 5: /leds+mosfets/frame7 -> /leds+mosfets/0frame7
- T4 pad 6: /leds+mosfets/frame7 -> /leds+mosfets/0frame7
- T4 pad 7: /leds+mosfets/frame8 -> /leds+mosfets/0frame8
- T4 pad 8: /leds+mosfets/frame8 -> /leds+mosfets/0frame8
- T5 pad 5: /leds+mosfets/frame9 -> /leds+mosfets/0frame9
- T5 pad 6: /leds+mosfets/frame9 -> /leds+mosfets/0frame9
- T5 pad 7: /leds+mosfets/frame10 -> /leds+mosfets/0frame10
- T5 pad 8: /leds+mosfets/frame10 -> /leds+mosfets/0frame10
- T6 pad 5: /leds+mosfets/frame11 -> /leds+mosfets/0frame11
- T6 pad 6: /leds+mosfets/frame11 -> /leds+mosfets/0frame11
- T6 pad 7: /leds+mosfets/frame12 -> /leds+mosfets/0frame12
- T6 pad 8: /leds+mosfets/frame12 -> /leds+mosfets/0frame12
- T7 pad 5: /leds+mosfets/frame13 -> /leds+mosfets/0frame13
- T7 pad 6: /leds+mosfets/frame13 -> /leds+mosfets/0frame13
- T7 pad 7: /leds+mosfets/frame14 -> /leds+mosfets/0frame14
- T7 pad 8: /leds+mosfets/frame14 -> /leds+mosfets/0frame14
- T8 pad 5: /leds+mosfets/frame15 -> /leds+mosfets/0frame15
- T8 pad 6: /leds+mosfets/frame15 -> /leds+mosfets/0frame15
- T8 pad 7: /leds+mosfets/frame16 -> /leds+mosfets/0frame16
- T8 pad 8: /leds+mosfets/frame16 -> /leds+mosfets/0frame16
- U1 pad 1: /leds+mosfets/5or6or7or8 -> /leds+mosfets/05or6or7or8
- U1 pad 10: /leds+mosfets/frame8 -> /leds+mosfets/0frame8
- U1 pad 11: /leds+mosfets/frame7 -> /leds+mosfets/0frame7
- U1 pad 12: /leds+mosfets/frame6 -> /leds+mosfets/0frame6
- U1 pad 13: /leds+mosfets/6or7or8 -> /leds+mosfets/06or7or8
- U1 pad 2: /leds+mosfets/frame5 -> /leds+mosfets/0frame5
- U1 pad 3: /leds+mosfets/frame6 -> /leds+mosfets/0frame6
- U1 pad 4: /leds+mosfets/frame7 -> /leds+mosfets/0frame7
- U1 pad 5: /leds+mosfets/frame8 -> /leds+mosfets/0frame8
- U2 pad 1: /leds+mosfets/frame10 -> /leds+mosfets/0frame10
- U2 pad 10: /leds+mosfets/16or1 -> /leds+mosfets/016or1
- U2 pad 11: /leds+mosfets/frame1 -> /leds+mosfets/0frame1
- U2 pad 12: /leds+mosfets/frame16 -> /leds+mosfets/0frame16
- U2 pad 2: /leds+mosfets/frame9 -> /leds+mosfets/0frame9
- U2 pad 3: /leds+mosfets/frame7 -> /leds+mosfets/0frame7
- U2 pad 4: /leds+mosfets/frame8 -> /leds+mosfets/0frame8
- U2 pad 5: /leds+mosfets/frame9 -> /leds+mosfets/0frame9
- U2 pad 6: /leds+mosfets/7or8or9 -> /leds+mosfets/07or8or9
- U2 pad 7: unconnected-(U2-VSS-Pad7) -> GND
- U2 pad 8: /leds+mosfets/frame8 -> /leds+mosfets/0frame8
- U2 pad 9: /leds+mosfets/8or9or10 -> /leds+mosfets/08or9or10
- U3 pad 1: /leds+mosfets/frame3 -> /leds+mosfets/0frame3
- U3 pad 10: /leds+mosfets/frame12 -> /leds+mosfets/0frame12
- U3 pad 11: /leds+mosfets/4or5 -> /leds+mosfets/04or5
- U3 pad 12: /leds+mosfets/frame5 -> /leds+mosfets/0frame5
- U3 pad 13: /leds+mosfets/frame4 -> /leds+mosfets/0frame4
- U3 pad 2: /leds+mosfets/frame4 -> /leds+mosfets/0frame4
- U3 pad 3: /leds+mosfets/3or4 -> /leds+mosfets/03or4
- U3 pad 4: /leds+mosfets/frame5 -> /leds+mosfets/0frame5
- U3 pad 5: /leds+mosfets/frame6 -> /leds+mosfets/0frame6
- U3 pad 6: /leds+mosfets/5or6 -> /leds+mosfets/05or6
- U3 pad 8: /leds+mosfets/12or13 -> /leds+mosfets/012or13
- U3 pad 9: /leds+mosfets/frame13 -> /leds+mosfets/0frame13
- U6 pad 1: /leds+mosfets/frame13 -> /leds+mosfets/0frame13
- U6 pad 10: /leds+mosfets/frame9 -> /leds+mosfets/0frame9
- U6 pad 11: /leds+mosfets/15or16 -> /leds+mosfets/015or16
- U6 pad 12: /leds+mosfets/frame16 -> /leds+mosfets/0frame16
- U6 pad 13: /leds+mosfets/frame15 -> /leds+mosfets/0frame15
- U6 pad 2: /leds+mosfets/frame14 -> /leds+mosfets/0frame14
- U6 pad 3: /leds+mosfets/13or14 -> /leds+mosfets/013or14
- U6 pad 4: /leds+mosfets/frame14 -> /leds+mosfets/0frame14
- U6 pad 5: /leds+mosfets/frame15 -> /leds+mosfets/0frame15
- U6 pad 6: /leds+mosfets/14or15 -> /leds+mosfets/014or15
- U6 pad 8: /leds+mosfets/9or10 -> /leds+mosfets/09or10
- U6 pad 9: /leds+mosfets/frame10 -> /leds+mosfets/0frame10
- U8 pad 1: /leds+mosfets/frame7 -> /leds+mosfets/0frame7
- U8 pad 11: /leds+mosfets/8or9 -> /leds+mosfets/08or9
- U8 pad 12: /leds+mosfets/frame9 -> /leds+mosfets/0frame9
- U8 pad 13: /leds+mosfets/frame8 -> /leds+mosfets/0frame8
- U8 pad 2: /leds+mosfets/frame8 -> /leds+mosfets/0frame8
- U8 pad 3: /leds+mosfets/7or8 -> /leds+mosfets/07or8
- U8 pad 4: /leds+mosfets/frame6 -> /leds+mosfets/0frame6
- U8 pad 5: /leds+mosfets/frame7 -> /leds+mosfets/0frame7
- U8 pad 6: /leds+mosfets/6or7 -> /leds+mosfets/06or7
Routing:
- net /leds+mosfets/7or8: track 22.5 -> 469.1 mm, vias 2 -> 7
- net /leds+mosfets/15or16: track 300.3 -> 0.00 mm, vias 4 -> 0
- net /leds+mosfets/frame15: track 278.2 -> 0.00 mm, vias 8 -> 0
- net /leds+mosfets/frame6: track 21.4 -> 245.5 mm, vias 0 -> 5
- net /leds+mosfets/13or14: track 219.5 -> 0.00 mm, vias 2 -> 0
- net /leds+mosfets/frame3: track 20.3 -> 220.4 mm, vias 0 -> 8
- net /leds+mosfets/frame1: track 1.27 -> 172.5 mm, vias 0 -> 3
- net /leds+mosfets/frame4: track 165.2 -> 0.00 mm, vias 8 -> 0
- net /leds+mosfets/4or5: track 396.1 -> 231.2 mm, vias 4 -> 0
- net /leds+mosfets/frame10: track 163.4 -> 0.00 mm, vias 6 -> 0
- net /leds+mosfets/0frame6: track 0.00 -> 136.5 mm, vias 0 -> 4
- net /leds+mosfets/14or15: track 131.4 -> 0.00 mm
- net /leds+mosfets/0frame9: track 0.00 -> 115.6 mm
- net /leds+mosfets/12or13: track 94.3 -> 0.00 mm, vias 2 -> 0
- net /leds+mosfets/frame14: track 81.8 -> 0.00 mm, vias 2 -> 0
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- added copper zone on In2.Cu, net +2V2
- added copper zone on F.Cu, net +3.3V
- added copper zone on F.Cu, net /leds+mosfets/0frame1
- added copper zone on F.Cu, net /leds+mosfets/0frame10
- added copper zone on F.Cu, net /leds+mosfets/0frame13
- added copper zone on F.Cu, net /leds+mosfets/0frame14
- added copper zone on F.Cu, net /leds+mosfets/0frame15
- added copper zone on F.Cu, net /leds+mosfets/0frame16
- added copper zone on F.Cu, net /leds+mosfets/0frame2
- added copper zone on F.Cu, net /leds+mosfets/0frame3
- added copper zone on F.Cu, net /leds+mosfets/0frame4
- added copper zone on F.Cu, net /leds+mosfets/0frame5
- added copper zone on F.Cu, net /leds+mosfets/0frame6
- added copper zone on F.Cu, net /leds+mosfets/0frame7
- added copper zone on F.Cu, net /leds+mosfets/0frame8
- added copper zone on F.Cu, net /leds+mosfets/0frame9
- added copper zone on F.Cu, net /pd_r_18/19
- added copper zone on F.Cu, net /u4-pu-r1
- added copper zone on F.Cu, net /u4-pu-r2
- added copper zone on F.Cu, net /u5-pu-r1
- added copper zone on F.Cu, net /u5-pu-r2
- added copper zone on In1.Cu, net GND
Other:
- copper layers 2 -> 4
